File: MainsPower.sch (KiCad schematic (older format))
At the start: 19 parts

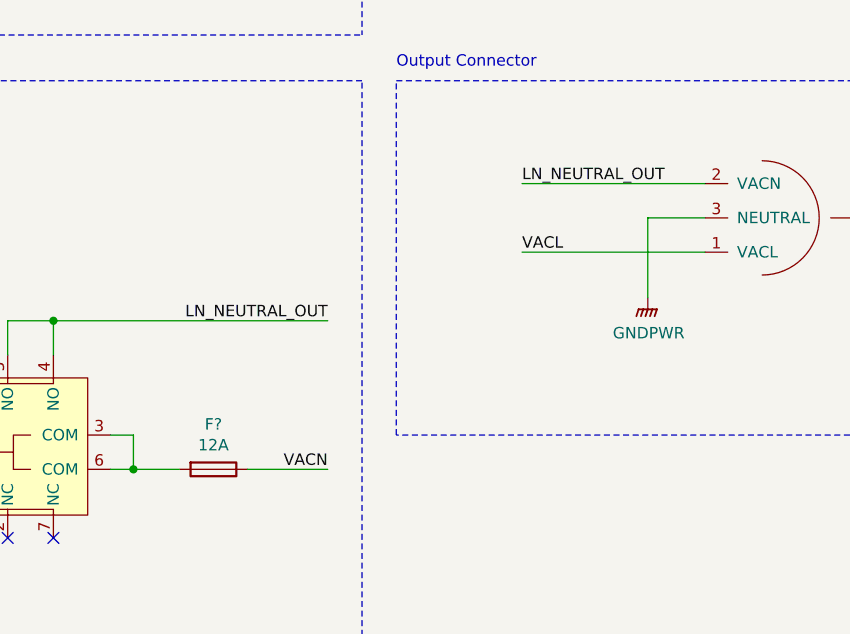
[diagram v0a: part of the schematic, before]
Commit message: Changed to breaking line instead of neutral
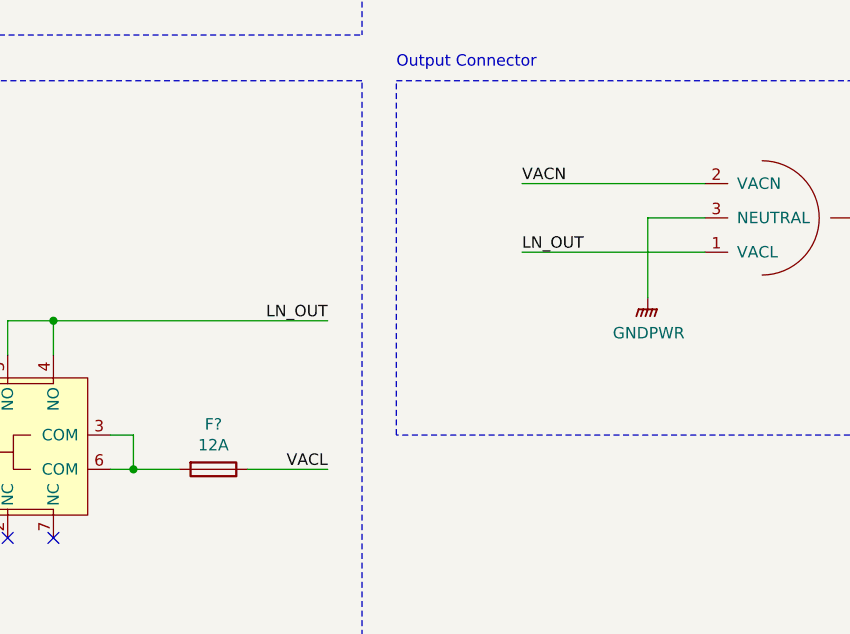
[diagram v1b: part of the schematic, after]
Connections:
- net VACL: now also F?.1; no longer J?.1 (VACL)
- net VACN: now also J?.2 (VACN); no longer F?.1
- net LN_NEUTRAL_OUT renamed LN_OUT
- net LN_OUT: now also J?.1 (VACL); no longer J?.2 (VACN)
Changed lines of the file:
@@
 	5300 4550 5200 4550
 Text Label 6150 4550 2    50   ~ 0
-VACN
+VACL
 Wire Wire Line
 	4750 4050 4750 3900
@@
 Connection ~ 4950 3900
 Text Label 6150 3900 2    50   ~ 0
-LN_NEUTRAL_OUT
+LN_OUT
 NoConn ~ 5650 2000
 $Comp
@@
 	7800 3300 7000 3300
 Text Label 7000 3300 0    50   ~ 0
-LN_NEUTRAL_OUT
+VACN
 Wire Wire Line
 	7800 3600 7000 3600
@@
 $EndComp
 Text Label 7000 3600 0    50   ~ 0
-VACL
+LN_OUT
 $Comp
 L ReflowOven:IEC320-C14 J?

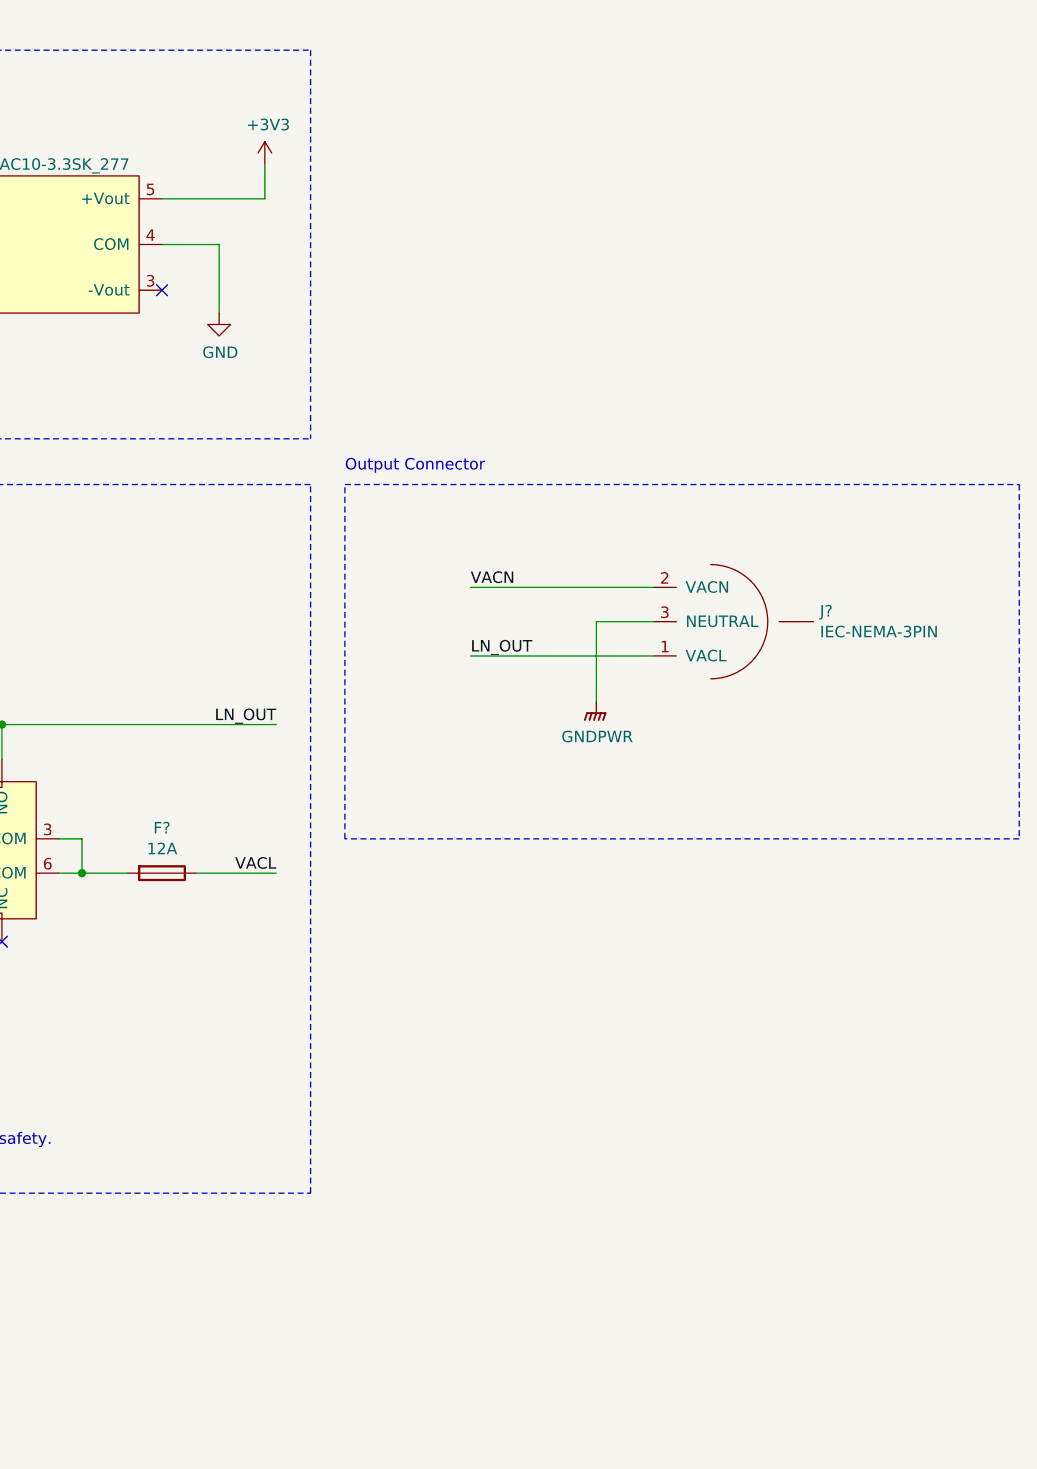
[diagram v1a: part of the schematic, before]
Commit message: Added temp circuit for current sense
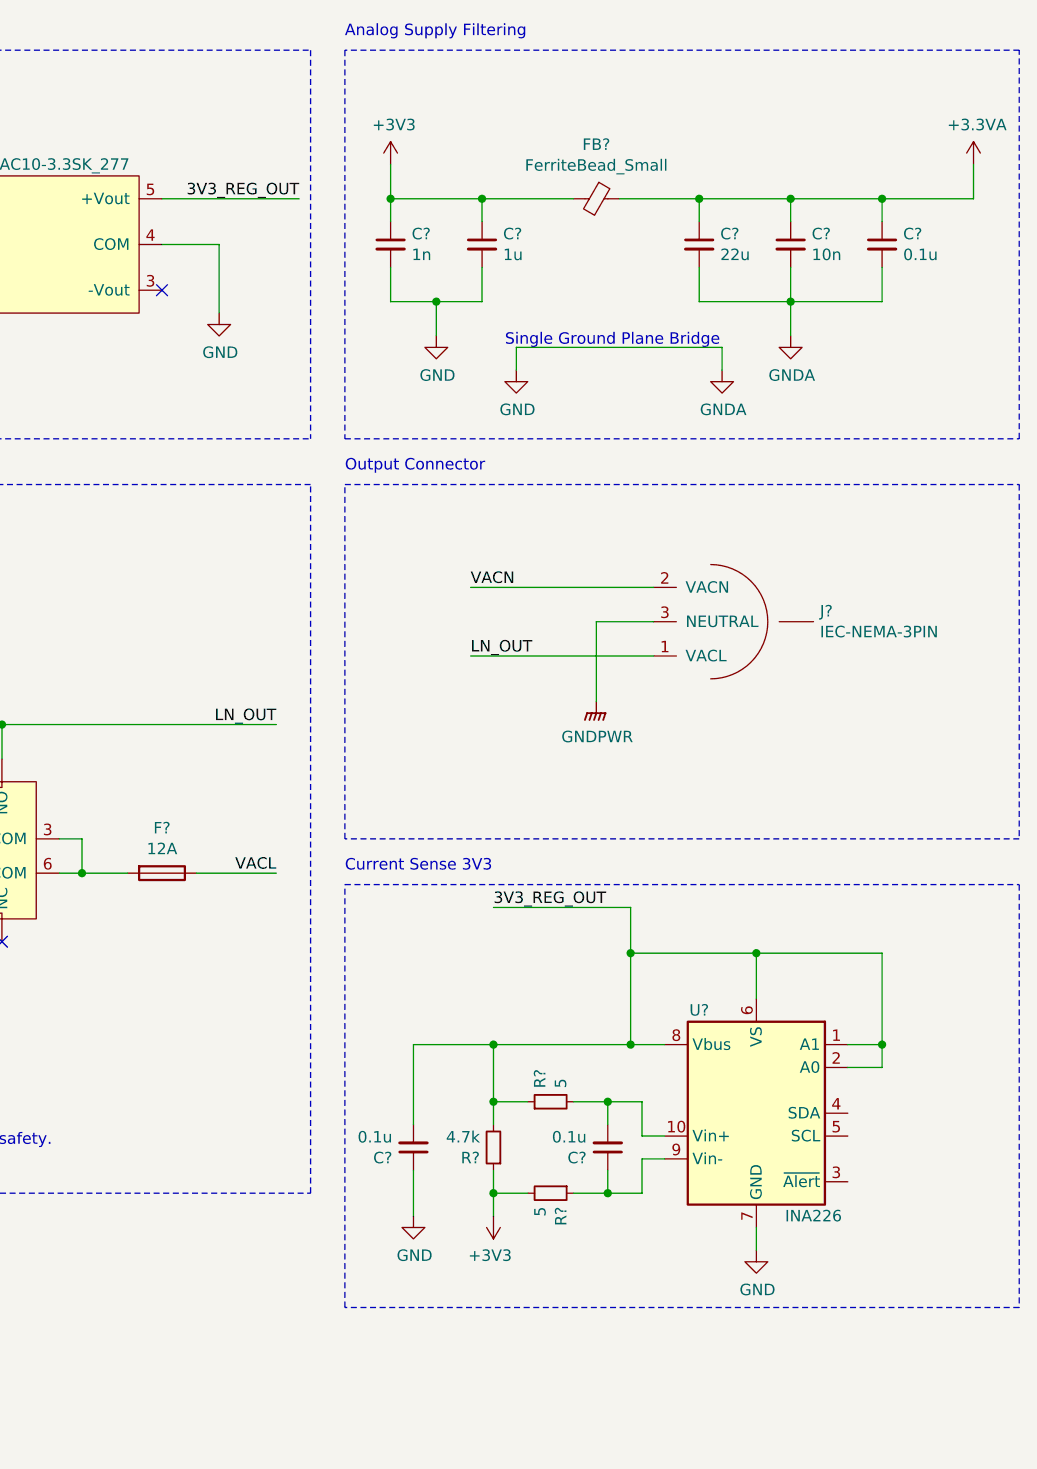
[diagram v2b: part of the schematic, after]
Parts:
- added C? (x3): 0.1u, Capacitor_SMD:C_0603_1608Metric, symbol Device:C_Small
- added C?: 1n, Capacitor_SMD:C_0603_1608Metri, symbol Device:C_Small
- added C?: 1u, Capacitor_SMD:C_0603_1608Metric, symbol Device:C_Small
- added C?: 22u, Capacitor_SMD:C_0603_1608Metric, symbol Device:C_Small
- added C?: 10n, Capacitor_SMD:C_0603_1608Metric, symbol Device:C_Small
- added FB?: FerriteBead_Small, symbol Device:FerriteBead_Small
- added R? (x2): 5, symbol Device:R_Small
- added R?: 4.7k, symbol Device:R_Small
- added U?: INA226, Package_SO:VSSOP-10_3x3mm_P0.5mm, symbol Analog_ADC:INA226
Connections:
- net +3V3: now also C?.1, C?.1, FB?.2, R?.1, R?.2; no longer P?.5 (+Vout)
- net GND: now also C?.1, C?.2, C?.2, C?.2, C?.2, C?.2, U?.7 (GND)
- new net: C?.2, R?.2, U?.10 (Vin+)
- new net: C?.1, R?.1, U?.9 (Vin-)
- new net +3.3VA: C?.1, C?.1, C?.1, FB?.1
- new net 3V3_REG_OUT: C?.2, P?.5 (+Vout), R?.1, R?.2, U?.1 (A1), U?.2 (A0), U?.6 (VS), U?.8 (Vbus)
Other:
- note added: "Analog Supply Filtering"
- note added: "Current Sense 3V3"
- note added: "Single Ground Plane Bridge"

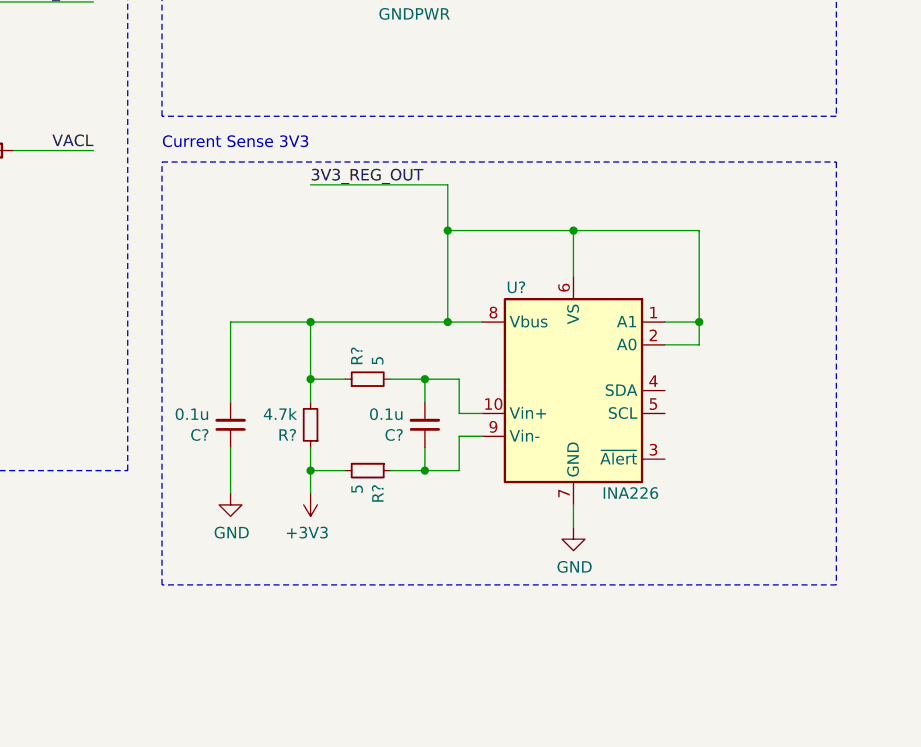
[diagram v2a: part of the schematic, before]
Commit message: Added current sense
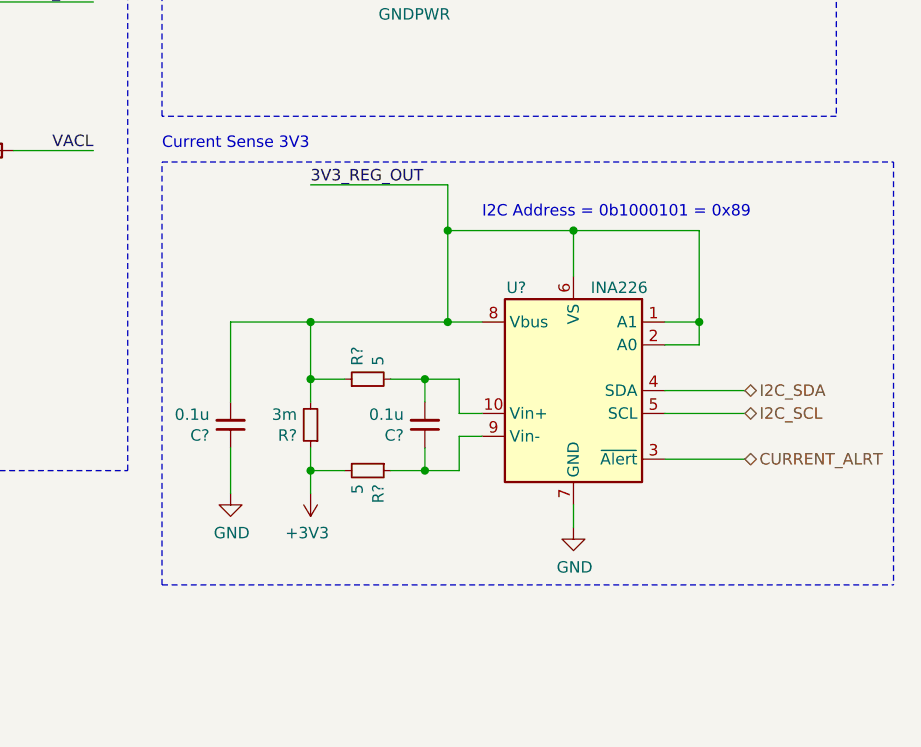
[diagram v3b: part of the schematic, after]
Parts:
- R?: value 4.7k -> 3m
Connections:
- net CURRENT_ALRT: now reaches U?.3 (~Alert~)
- net I2C_SDA: now reaches U?.4 (SDA)
- net I2C_SCL: now reaches U?.5 (SCL)
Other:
- note added: "I2C Address = 0b1000101 = 0x89"
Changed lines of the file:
@@
 P 8250 5600
 F 0 "U?" H 8000 6050 50  0000 C CNN
-F 1 "INA226" H 8500 5150 50  0000 C CNN
+F 1 "INA226" H 8450 6050 50  0000 C CNN
 F 2 "Package_SO:VSSOP-10_3x3mm_P0.5mm" H 9050 5150 50  0001 C CNN
 F 3 "http://www.ti.com/lit/ds/symlink/ina226.pdf" H 8600 5500 50  0001 C CNN
@@
 P 7100 5750
 F 0 "R?" H 7159 5796 50  0000 L CNN
-F 1 "4.7k" H 7159 5705 50  0000 L CNN
+F 1 "3m" H 7159 5705 50  0000 L CNN
 F 2 "" H 7100 5750 50  0001 C CNN
 F 3 "~" H 7100 5750 50  0001 C CNN
@@
 	8250 6200 8250 6100
 Wire Notes Line
-	6450 4600 9400 4600
-Wire Notes Line
-	9400 4600 9400 6450
-Wire Notes Line
-	9400 6450 6450 6450
+	9650 4600 9650 6450
 Wire Notes Line
 	6450 6450 6450 4600
@@
 Wire Wire Line
 	8800 5300 8800 4900
+Text Notes 7850 4850 0    50   ~ 0
+I2C Address = 0b1000101 = 0x89
+Wire Wire Line
+	8650 5600 9000 5600
+Wire Wire Line
+	8650 5700 9000 5700
+Wire Wire Line
+	8650 5900 9000 5900
+Text HLabel 9000 5600 2    50   BiDi ~ 0
+I2C_SDA
+Text HLabel 9000 5700 2    50   BiDi ~ 0
+I2C_SCL
+Text HLabel 9000 5900 2    50   BiDi ~ 0
+CURRENT_ALRT
+Wire Notes Line
+	6450 6450 9650 6450
+Wire Notes Line
+	6450 4600 9650 4600
 $EndSCHEMATC

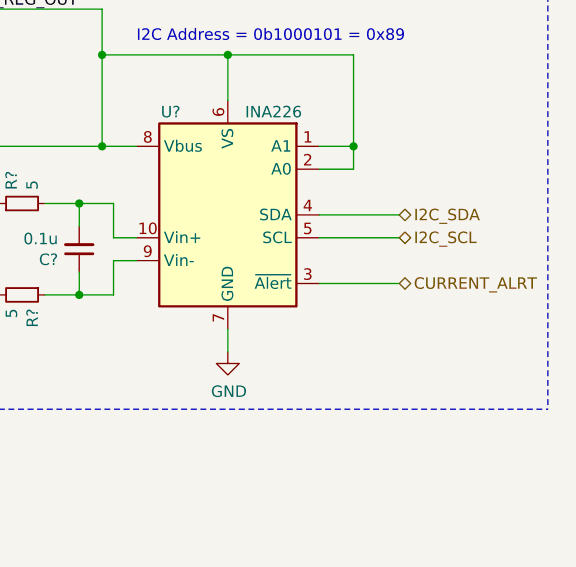
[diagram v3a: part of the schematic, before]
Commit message: Added communication interfaces
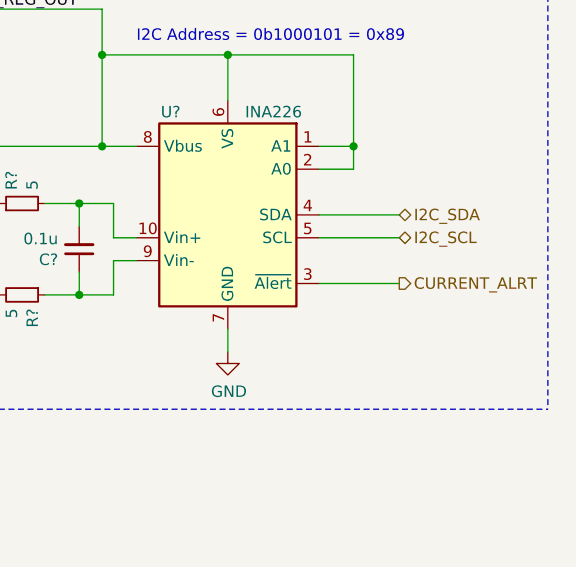
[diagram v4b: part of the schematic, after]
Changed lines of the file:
@@
 $Descr A4 11693 8268
 encoding utf-8
-Sheet 1 1
+Sheet 1 6
 Title ""
 Date ""
@@
 Text HLabel 9000 5700 2    50   BiDi ~ 0
 I2C_SCL
-Text HLabel 9000 5900 2    50   BiDi ~ 0
+Text HLabel 9000 5900 2    50   Output ~ 0
 CURRENT_ALRT
 Wire Notes Line

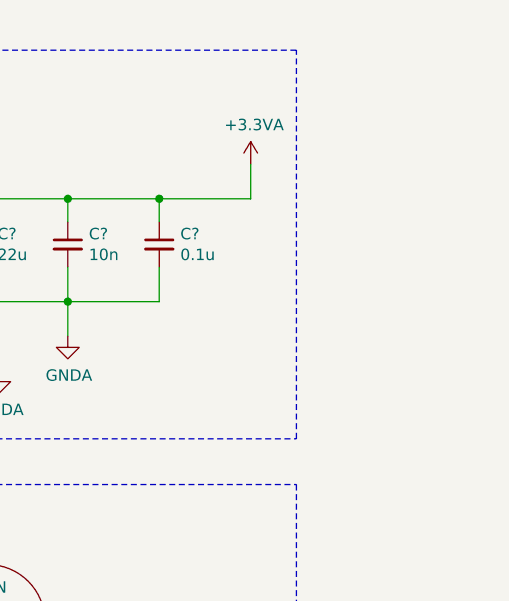
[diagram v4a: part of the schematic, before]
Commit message: Preliminary Microcontroller schematic done
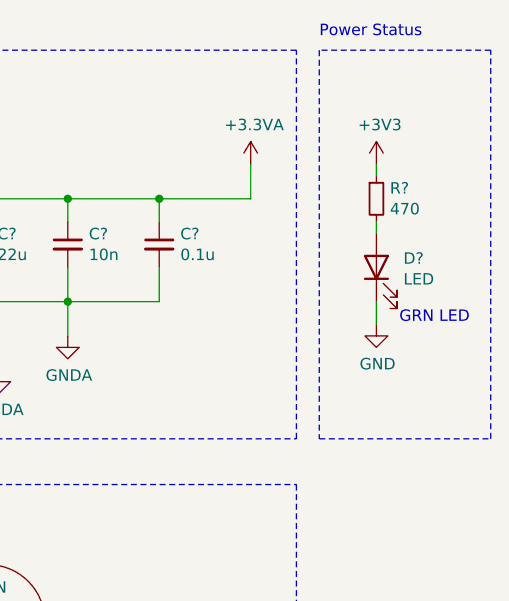
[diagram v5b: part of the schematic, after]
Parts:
- added D?: LED, symbol Device:LED
- added R?: 470, symbol Device:R_Small
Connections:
- net +3V3: now also R?.1
- net GND: now also D?.1 (K)
- new net: D?.2 (A), R?.2
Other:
- note added: "GRN LED"
- note added: "Power Status"
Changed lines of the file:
@@
 $Descr A4 11693 8268
 encoding utf-8
-Sheet 1 6
+Sheet 1 1
 Title ""
 Date ""
@@
 Wire Notes Line
 	6450 4600 9650 4600
+$Comp
+L power:+3V3 #PWR?
+U 1 1 5F685D62
+P 9750 1450
+F 0 "#PWR?" H 9750 1300 50  0001 C CNN
+F 1 "+3V3" H 9765 1623 50  0000 C CNN
+F 2 "" H 9750 1450 50  0001 C CNN
+F 3 "" H 9750 1450 50  0001 C CNN
+	1    9750 1450
+	1    0    0    -1
+$EndComp
+$Comp
+L Device:LED D?
+U 1 1 5F68672E
+P 9750 1900
+F 0 "D?" V 9789 1782 50  0000 R CNN
+F 1 "LED" V 9698 1782 50  0000 R CNN
+F 2 "" H 9750 1900 50  0001 C CNN
+F 3 "~" H 9750 1900 50  0001 C CNN
+	1    9750 1900
+	0    -1   -1   0
+$EndComp
+$Comp
+L power:GND #PWR?
+U 1 1 5F686DA9
+P 9750 2150
+F 0 "#PWR?" H 9750 1900 50  0001 C CNN
+F 1 "GND" H 9755 1977 50  0000 C CNN
+F 2 "" H 9750 2150 50  0001 C CNN
+F 3 "" H 9750 2150 50  0001 C CNN
+	1    9750 2150
+	1    0    0    -1
+$EndComp
+Wire Wire Line
+	9750 2150 9750 2050
+Text Notes 9850 2150 0    50   ~ 0
+GRN LED
+$Comp
+L Device:R_Small R?
+U 1 1 5F68D65A
+P 9750 1600
+F 0 "R?" H 9809 1646 50  0000 L CNN
+F 1 "470" H 9809 1555 50  0000 L CNN
+F 2 "" H 9750 1600 50  0001 C CNN
+F 3 "~" H 9750 1600 50  0001 C CNN
+	1    9750 1600
+	1    0    0    -1
+$EndComp
+Wire Wire Line
+	9750 1500 9750 1450
+Wire Wire Line
+	9750 1700 9750 1750
+Wire Notes Line
+	9500 950  9500 2650
+Wire Notes Line
+	9500 2650 10250 2650
+Wire Notes Line
+	10250 2650 10250 950
+Wire Notes Line
+	10250 950  9500 950
+Text Notes 9500 900  0    50   ~ 0
+Power Status
 $EndSCHEMATC

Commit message: Done with preliminary schematic. Needs review
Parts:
- C501: renamed from C?; footprint Capacitor_SMD:C_0603_1608Metri -> Capacitor_SMD:C_0603_1608Metric
- C517, C518: renamed from C?; footprint Capacitor_SMD:C_0603_1608Metric -> (none)
- R501, R502, R503, R505: renamed from R?; footprint (none) -> Resistor_SMD:R_0603_1608Metric
- gave numbers to parts that had none: 26
